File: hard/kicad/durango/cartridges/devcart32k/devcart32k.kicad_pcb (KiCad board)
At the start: 2 copper layers, 114.3 x 53.3 mm, 12 parts, among them J1 to Computer, J2 SD Interface, U1 27/28C256, U2 62256, U4 74HC174, U5 74HC139, U6 74HC245, U7 74HC139

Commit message: revise devcart PCB
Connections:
- U2 pad 27: /~WE -> /G~WE
- U5 pad 5: (no net) -> /~STATUS
- U5 pad 6: /~STATUS -> (no net)
- U7 pad 4: /~WE -> /G~WE
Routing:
- net /G~WE: track 0.00 -> 20.1 mm
- net /~WE: track 78.2 -> 77.6 mm
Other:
- board text added: "Durango 32 KiB Developer SD-card cartridge v2"
- board text added: "Revised 2023·01·22"
- board text added: "Serial No."
- board text removed: "Durango 32 KiB Developer SD-card cartridge v1"
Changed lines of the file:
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@@
   (general
     (thickness 1.6)
-    (drawings 32)
-    (tracks 521)
+    (drawings 35)
+    (tracks 523)
     (zones 0)
     (modules 12)
-    (nets 41)
+    (nets 42)
   )
   (page A4)
@@
   (net 39 /~LATCH)
   (net 40 /~STATUS)
+  (net 41 /G~WE)
   (net_class Default "Esta es la clase de red por defecto."
     (clearance 0.2)
@@
     (uvia_dia 0.3)
     (uvia_drill 0.1)
+    (add_net /G~WE)
     (add_net /MCLK)
     (add_net /MISO)
@@
     (pad 12 thru_hole oval (at 7.62 10.16) (size 1.6 1.6) (drill 0.8) (layers *.Cu *.Mask))
     (pad 4 thru_hole oval (at 0 7.62) (size 1.6 1.6) (drill 0.8) (layers *.Cu *.Mask)
-      (net 17 /~WE))
+      (net 41 /G~WE))
     (pad 11 thru_hole oval (at 7.62 12.7) (size 1.6 1.6) (drill 0.8) (layers *.Cu *.Mask)
       (net 35 /ROM~OE))
@@
     (pad 14 thru_hole oval (at 7.62 5.08) (size 1.6 1.6) (drill 0.8) (layers *.Cu *.Mask)
       (net 4 +5V))
-    (pad 6 thru_hole oval (at 0 12.7) (size 1.6 1.6) (drill 0.8) (layers *.Cu *.Mask)
-      (net 40 /~STATUS))
+    (pad 6 thru_hole oval (at 0 12.7) (size 1.6 1.6) (drill 0.8) (layers *.Cu *.Mask))
     (pad 13 thru_hole oval (at 7.62 7.62) (size 1.6 1.6) (drill 0.8) (layers *.Cu *.Mask)
       (net 4 +5V))
-    (pad 5 thru_hole oval (at 0 10.16) (size 1.6 1.6) (drill 0.8) (layers *.Cu *.Mask))
+    (pad 5 thru_hole oval (at 0 10.16) (size 1.6 1.6) (drill 0.8) (layers *.Cu *.Mask)
+      (net 40 /~STATUS))
     (pad 12 thru_hole oval (at 7.62 10.16) (size 1.6 1.6) (drill 0.8) (layers *.Cu *.Mask))
     (pad 4 thru_hole oval (at 0 7.62) (size 1.6 1.6) (drill 0.8) (layers *.Cu *.Mask)
@@
       (net 1 GND))
     (pad 27 thru_hole oval (at 15.24 2.54 180) (size 1.6 1.6) (drill 0.8) (layers *.Cu *.Mask)
-      (net 17 /~WE))
+      (net 41 /G~WE))
     (pad 13 thru_hole oval (at 0 30.48 180) (size 1.6 1.6) (drill 0.8) (layers *.Cu *.Mask)
       (net 5 D2))
@@
     (pad 1 smd roundrect (at 45.72 -3.81 270) (size 1.524 8) (layers F.Cu F.Paste F.Mask) (roundrect_rratio 0.25))
   )
+  (gr_text "Serial No." (at 138.43 119.38 270) (layer B.SilkS)
+    (effects (font (size 1 1) (thickness 0.15)) (justify mirror))
+  )
+  (gr_poly (pts (xy 130.81 113.03) (xy 130.81 125.73) (xy 137.16 125.73) (xy 137.16 113.03)) (layer B.SilkS) (width 0.1))
+  (gr_text "Revised 2023·01·22" (at 149.225 125.73) (layer F.SilkS)
+    (effects (font (size 1.016 1.016) (thickness 0.16)))
+  )
   (gr_arc (start 52.324 117.094) (end 52.324 116.84) (angle -90) (layer Edge.Cuts) (width 0.05))
   (gr_arc (start 52.324 114.046) (end 52.07 114.046) (angle -90) (layer Edge.Cuts) (width 0.05))
@@
     (effects (font (size 1.27 1.016) (thickness 0.254)))
   )
-  (gr_text "Durango 32 KiB Developer SD-card cartridge v1" (at 62.865 94.615 270) (layer F.SilkS)
+  (gr_text "Durango 32 KiB Developer SD-card cartridge v2" (at 62.865 94.615 270) (layer F.SilkS)
     (effects (font (size 1.016 1.016) (thickness 0.16)))
   )
@@
   (segment (start 119.38 106.68) (end 110.49 106.68) (width 0.25) (layer B.Cu) (net 17))
   (segment (start 120.65 107.95) (end 119.38 106.68) (width 0.25) (layer B.Cu) (net 17))
-  (segment (start 107.315 111.125) (end 108.420001 112.230001) (width 0.25) (layer F.Cu) (net 17))
-  (segment (start 108.420001 112.230001) (end 109.22 113.03) (width 0.25) (layer F.Cu) (net 17))
-  (segment (start 107.315 109.855) (end 107.315 111.125) (width 0.25) (layer F.Cu) (net 17))
-  (segment (start 109.22 107.95) (end 107.315 109.855) (width 0.25) (layer F.Cu) (net 17))
-  (segment (start 107.95 114.3) (end 109.22 113.03) (width 0.25) (layer B.Cu) (net 17))
-  (segment (start 92.71 114.3) (end 107.95 114.3) (width 0.25) (layer B.Cu) (net 17))
-  (segment (start 92.71 114.3) (end 91.44 113.03) (width 0.25) (layer B.Cu) (net 17))
-  (segment (start 91.44 113.03) (end 90.17 113.03) (width 0.25) (layer B.Cu) (net 17))
+  (segment (start 107.95 114.3) (end 109.22 113.03) (width 0.25) (layer B.Cu) (net 41))
+  (segment (start 92.71 114.3) (end 107.95 114.3) (width 0.25) (layer B.Cu) (net 41))
+  (segment (start 92.71 114.3) (end 91.44 113.03) (width 0.25) (layer B.Cu) (net 41))
+  (segment (start 91.44 113.03) (end 90.17 113.03) (width 0.25) (layer B.Cu) (net 41))
   (segment (start 55.88 113.03) (end 64.77 113.03) (width 0.25) (layer B.Cu) (net 17))
   (segment (start 64.77 113.03) (end 66.04 114.3) (width 0.25) (layer B.Cu) (net 17))
@@
   (segment (start 66.04 115.57) (end 67.31 116.84) (width 0.25) (layer B.Cu) (net 17))
   (segment (start 67.31 116.84) (end 87.63 116.84) (width 0.25) (layer B.Cu) (net 17))
-  (via (at 87.63 116.84) (size 0.8) (drill 0.4) (layers F.Cu B.Cu) (net 17))
-  (segment (start 87.63 116.84) (end 87.63 115.57) (width 0.25) (layer F.Cu) (net 17))
-  (segment (start 87.63 115.57) (end 90.17 113.03) (width 0.25) (layer F.Cu) (net 17))
+  (segment (start 92.10501 117.41501) (end 92.71 118.02) (width 0.25) (layer B.Cu) (net 17))
+  (segment (start 88.20501 117.41501) (end 92.10501 117.41501) (width 0.25) (layer B.Cu) (net 17))
+  (segment (start 87.63 116.84) (end 88.20501 117.41501) (width 0.25) (layer B.Cu) (net 17))
+  (via (at 107.315 118.02) (size 0.8) (drill 0.4) (layers F.Cu B.Cu) (net 17))
+  (segment (start 92.71 118.02) (end 107.315 118.02) (width 0.25) (layer B.Cu) (net 17))
+  (segment (start 107.315 109.855) (end 109.22 107.95) (width 0.25) (layer F.Cu) (net 17))
+  (segment (start 107.315 118.02) (end 107.315 109.855) (width 0.25) (layer F.Cu) (net 17))
   (segment (start 119.6 80.01) (end 118.33 78.74) (width 0.25) (layer B.Cu) (net 18))
   (segment (start 120.65 80.01) (end 119.6 80.01) (width 0.25) (layer B.Cu) (net 18))
@@
   (segment (start 71.1 101.6) (end 71.1 118.09) (width 0.25) (layer F.Cu) (net 35))
   (via (at 71.1 118.09) (size 0.8) (drill 0.4) (layers F.Cu B.Cu) (net 35))
-  (segment (start 71.1 118.09) (end 106.66 118.09) (width 0.25) (layer B.Cu) (net 35))
-  (segment (start 106.66 118.09) (end 107.95 119.38) (width 0.25) (layer B.Cu) (net 35))
-  (segment (start 107.95 119.38) (end 115.57 119.38) (width 0.25) (layer B.Cu) (net 35))
+  (segment (start 91.42 118.09) (end 71.1 118.09) (width 0.25) (layer B.Cu) (net 35))
+  (segment (start 92.075 118.745) (end 91.42 118.09) (width 0.25) (layer B.Cu) (net 35))
+  (segment (start 106.045 118.745) (end 92.075 118.745) (width 0.25) (layer B.Cu) (net 35))
   (segment (start 115.57 119.38) (end 116.84 118.11) (width 0.25) (layer B.Cu) (net 35))
+  (segment (start 106.68 119.38) (end 115.57 119.38) (width 0.25) (layer B.Cu) (net 35))
+  (segment (start 106.045 118.745) (end 106.68 119.38) (width 0.25) (layer B.Cu) (net 35))
   (segment (start 107.95 121.92) (end 115.57 121.92) (width 0.25) (layer B.Cu) (net 36))
   (segment (start 115.57 121.92) (end 116.84 123.19) (width 0.25) (layer B.Cu) (net 36))
@@
   (segment (start 129.54 109.22) (end 129.54 99.06) (width 0.25) (layer F.Cu) (net 39))
   (segment (start 129.54 99.06) (end 128.27 97.79) (width 0.25) (layer F.Cu) (net 39))
-  (segment (start 119.38 116.84) (end 120.65 118.11) (width 0.25) (layer F.Cu) (net 40))
   (segment (start 116.205 116.84) (end 119.38 116.84) (width 0.25) (layer F.Cu) (net 40))
   (segment (start 115.429999 117.615001) (end 116.205 116.84) (width 0.25) (layer F.Cu) (net 40))
@@
   (segment (start 114.440001 117.615001) (end 115.429999 117.615001) (width 0.25) (layer F.Cu) (net 40))
   (segment (start 116.84 80.01) (end 113.665 83.185) (width 0.25) (layer F.Cu) (net 40))
+  (segment (start 119.38 116.84) (end 120.65 115.57) (width 0.25) (layer F.Cu) (net 40))
   (zone (net 1) (net_name GND) (layer F.Cu) (hatch edge 0.508)
     (connect_pads (clearance 0.508))

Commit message: fully revised devCart
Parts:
- C1: value 100n -> 22n
- LOGO1: moved to B.Cu
- LOGO3: moved to F.Cu
- moved LOGO1 2.54 mm to (147.3, 104.1), turned to 90 degrees
- moved LOGO3 1.42 mm to (158.1, 102.9), turned to 270 degrees
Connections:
- J1 pad 1: (no net) -> Net-(J1-Pad1)
- J1 pad 2: (no net) -> Net-(J1-Pad2)
- J1 pad 36: (no net) -> Net-(J1-Pad36)
- J1 pad 4: (no net) -> Net-(J1-Pad4)
- J2 pad 3: (no net) -> Net-(J2-Pad3)
- J2 pad 4: (no net) -> Net-(J2-Pad4)
- U4 pad 15: (no net) -> Net-(U4-Pad15)
- U5 pad 1: /~IOC -> /~BL0
- U5 pad 10: (no net) -> Net-(U5-Pad10)
- U5 pad 11: (no net) -> Net-(U5-Pad11)
- U5 pad 12: (no net) -> /~BL0
- U5 pad 13: +5V -> A5
- U5 pad 14: +5V -> A4
- U5 pad 15: +5V -> /~IOC
- U5 pad 3: GND -> A3
- U5 pad 6: (no net) -> Net-(U5-Pad6)
- U5 pad 7: (no net) -> Net-(U5-Pad7)
- U5 pad 9: (no net) -> Net-(U5-Pad9)
- U7 pad 10: (no net) -> Net-(U7-Pad10)
- U7 pad 12: (no net) -> Net-(U7-Pad12)
- U7 pad 5: (no net) -> Net-(U7-Pad5)
- U7 pad 6: (no net) -> Net-(U7-Pad6)
- U7 pad 7: (no net) -> Net-(U7-Pad7)
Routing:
- net A4: track 51.5 -> 87.4 mm, vias 0 -> 1
- net A5: track 51.5 -> 83.0 mm, vias 0 -> 2
- net A3: track 51.5 -> 80.4 mm, vias 0 -> 1
- net GND: track 202.9 -> 179.7 mm
- net /~BL0: track 0.00 -> 22.4 mm, vias 0 -> 1
- net +5V: track 179.8 -> 172.2 mm
- net /~IOC: track 95.8 -> 94.7 mm, vias 3 -> 2
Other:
- board text added: "Revised 2023·06·14"
- board text removed: "Revised 2023·01·22"

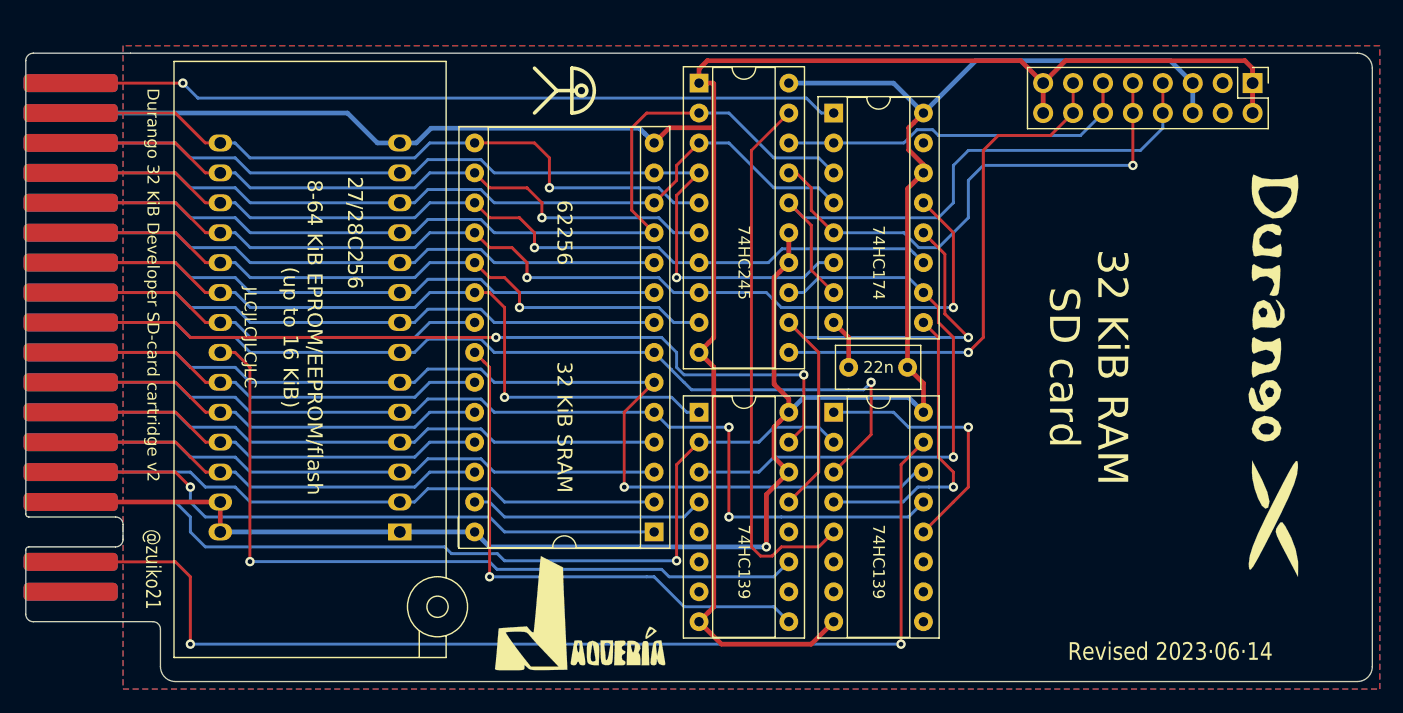
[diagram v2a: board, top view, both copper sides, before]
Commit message: faster timing and cleanup for DevCart
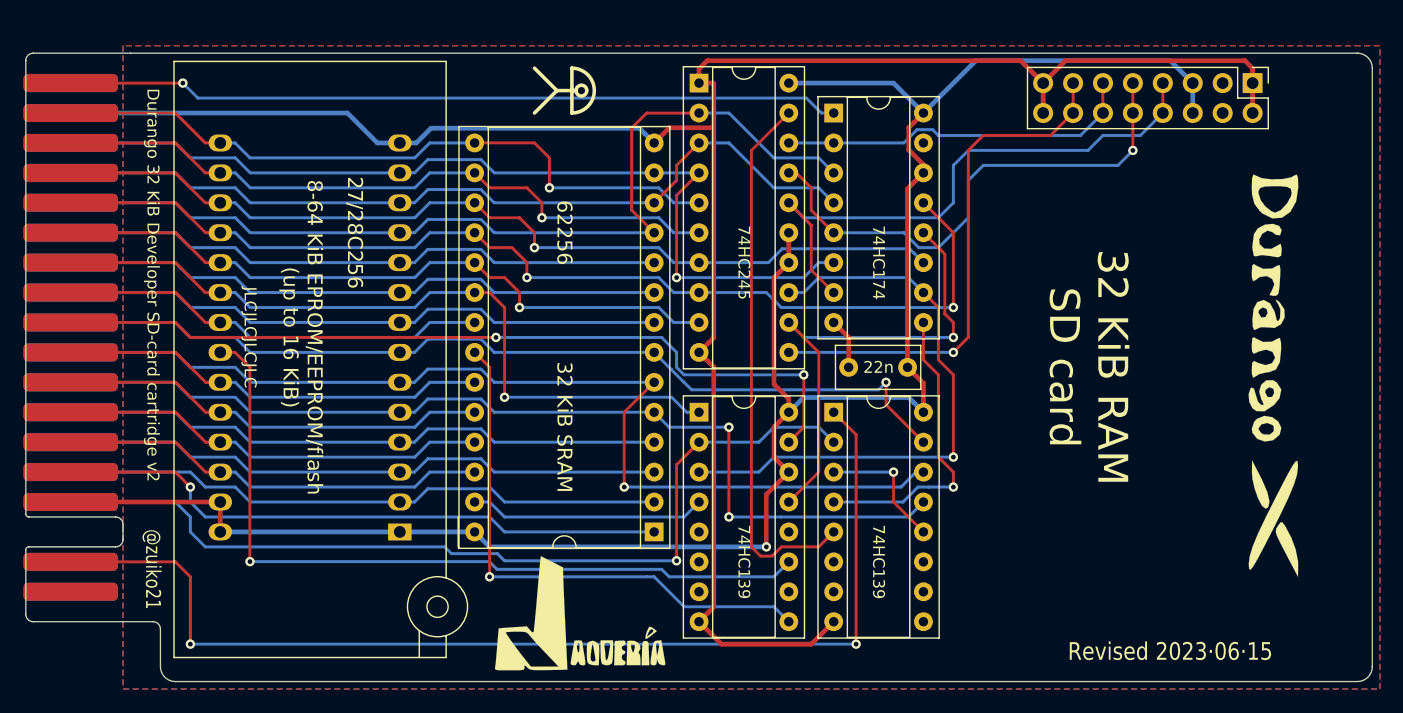
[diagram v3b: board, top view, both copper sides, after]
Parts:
- moved LOGO1 1.27 mm to (147.3, 102.9)
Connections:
- U5 pad 1: /~BL0 -> /~IOC
- U5 pad 15: /~IOC -> A3
- U5 pad 3: A3 -> /~BL0
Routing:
- net /~BL0: track 22.4 -> 11.2 mm
- net /~ROMEN: track 43.6 -> 41.8 mm
- net /~IOC: track 94.7 -> 93.4 mm
- net A3: track 80.4 -> 79.2 mm
- net /MOSI: track 44.7 -> 44.0 mm
- net /~SSEL: track 50.3 -> 49.6 mm
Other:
- board text added: "Revised 2023·06·15"
- board text removed: "Revised 2023·06·14"

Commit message: updated PCBs
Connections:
- J1 pad 1: Net-(J1-Pad1) -> (no net)
- J1 pad 2: Net-(J1-Pad2) -> (no net)
- J1 pad 36: Net-(J1-Pad36) -> (no net)
- J1 pad 4: Net-(J1-Pad4) -> (no net)
- J2 pad 3: Net-(J2-Pad3) -> (no net)
- J2 pad 4: Net-(J2-Pad4) -> (no net)
- U4 pad 15: Net-(U4-Pad15) -> (no net)
- U5 pad 10: Net-(U5-Pad10) -> (no net)
- U5 pad 11: Net-(U5-Pad11) -> (no net)
- U5 pad 6: Net-(U5-Pad6) -> (no net)
- U5 pad 7: Net-(U5-Pad7) -> (no net)
- U5 pad 9: Net-(U5-Pad9) -> (no net)
- U7 pad 10: Net-(U7-Pad10) -> (no net)
- U7 pad 12: Net-(U7-Pad12) -> (no net)
- U7 pad 5: Net-(U7-Pad5) -> (no net)
- U7 pad 6: Net-(U7-Pad6) -> (no net)
- U7 pad 7: Net-(U7-Pad7) -> (no net)
